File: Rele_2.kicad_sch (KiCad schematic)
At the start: 5 parts

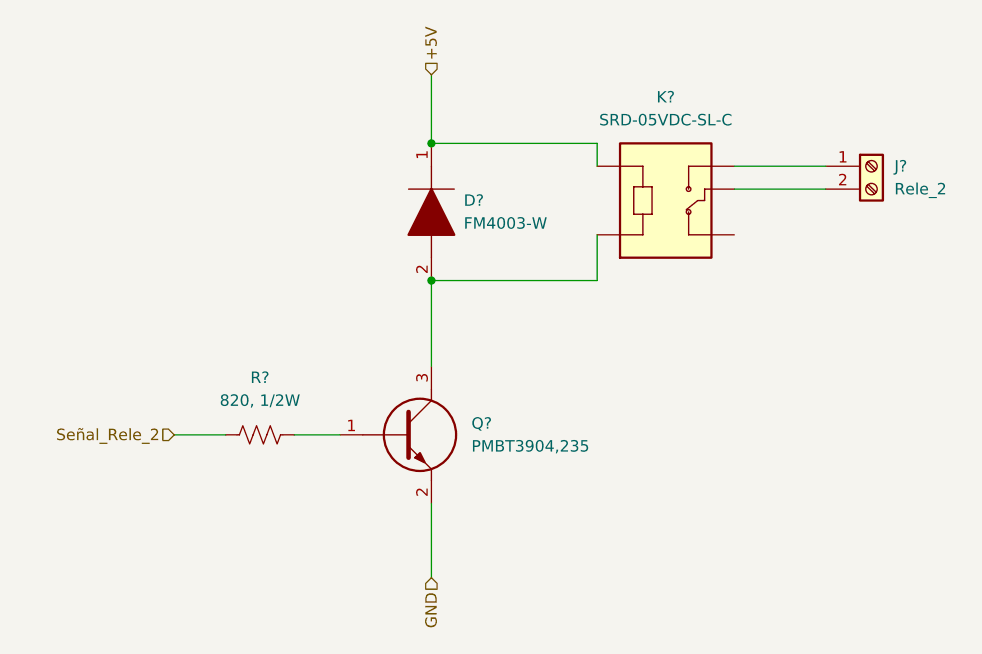
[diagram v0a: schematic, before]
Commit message: Ajuste del esquematico
Se cambio el integrado ESP32 por 2 tiras de pines de 1x15, se quitaron los switches EN y BOOT que ya estan en el NodeMCU, se quito el mutliplexor 74HC y se cablearon las I/O
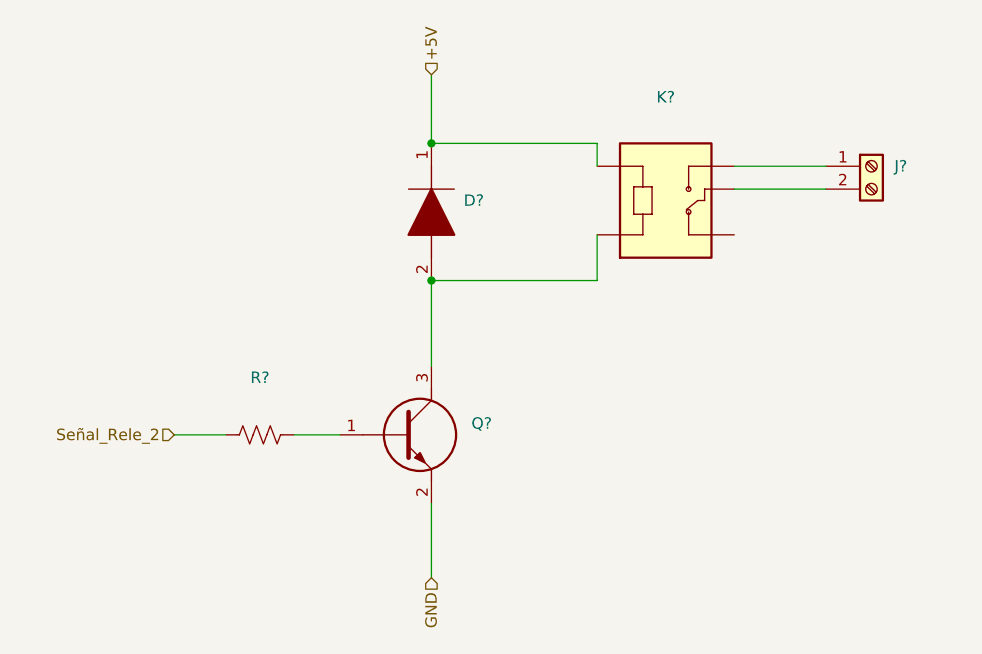
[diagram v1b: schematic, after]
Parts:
- D?: value FM4003-W -> (none); footprint DIOM5025X231N -> (none)
- J?: value Rele_2 -> (none)
- K?: value SRD-05VDC-SL-C -> (none); footprint RELAY_SRD-05VDC-SL-C -> (none)
- Q?: value PMBT3904,235 -> (none); footprint SOT95P230X110-3N -> (none)
- R?: value 820, 1/2W -> (none)
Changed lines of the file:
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@@
       (effects (font (size 1.27 1.27)) (justify left))
     )
-    (property "Value" "FM4003-W" (id 1) (at 142.6464 81.2799 90)
+    (property "Value" "" (id 1) (at 142.6464 81.2799 90)
       (effects (font (size 1.27 1.27)) (justify left))
     )
-    (property "Footprint" "DIOM5025X231N" (id 2) (at 139.065 83.82 0)
+    (property "Footprint" "" (id 2) (at 139.065 83.82 0)
       (effects (font (size 1.27 1.27)) (justify left) hide)
     )
@@
       (effects (font (size 1.27 1.27)) (justify left))
     )
-    (property "Value" "Rele_2" (id 1) (at 190.5 77.4699 0)
+    (property "Value" "" (id 1) (at 190.5 77.4699 0)
       (effects (font (size 1.27 1.27)) (justify left))
     )
@@
     (in_bom yes) (on_board yes) (fields_autoplaced)
     (property "Reference" "K?" (id 0) (at 165.1 67.2592 0))
-    (property "Value" "SRD-05VDC-SL-C" (id 1) (at 165.1 69.7992 0))
-    (property "Footprint" "RELAY_SRD-05VDC-SL-C" (id 2) (at 165.1 77.47 0)
+    (property "Value" "" (id 1) (at 165.1 69.7992 0))
+    (property "Footprint" "" (id 2) (at 165.1 77.47 0)
       (effects (font (size 1.27 1.27)) (justify left bottom) hide)
     )
@@
       (effects (font (size 1.27 1.27)) (justify left))
     )
-    (property "Value" "PMBT3904,235" (id 1) (at 143.51 106.0449 0)
+    (property "Value" "" (id 1) (at 143.51 106.0449 0)
       (effects (font (size 1.27 1.27)) (justify left))
     )
-    (property "Footprint" "SOT95P230X110-3N" (id 2) (at 142.875 108.585 0)
+    (property "Footprint" "" (id 2) (at 142.875 108.585 0)
       (effects (font (size 1.27 1.27)) (justify left) hide)
     )
@@
     (in_bom yes) (on_board yes) (fields_autoplaced)
     (property "Reference" "R?" (id 0) (at 120.015 98.425 90))
-    (property "Value" "820, 1/2W" (id 1) (at 120.015 100.965 90))
+    (property "Value" "" (id 1) (at 120.015 100.965 90))
     (property "Footprint" "" (id 2) (at 120.269 103.759 90)
       (effects (font (size 1.27 1.27)) hide)

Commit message: Modificación de posición de circ. filtrado y circ. de adaptación de tensión
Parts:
- D?, J?, K?, Q?, R?: value (none) -> ~
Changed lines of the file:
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@@
       (effects (font (size 1.27 1.27)) (justify left))
     )
-    (property "Value" "" (id 1) (at 142.6464 81.2799 90)
+    (property "Value" "~" (id 1) (at 142.6464 81.2799 90)
       (effects (font (size 1.27 1.27)) (justify left))
     )
@@
       (effects (font (size 1.27 1.27)) (justify left))
     )
-    (property "Value" "" (id 1) (at 190.5 77.4699 0)
+    (property "Value" "~" (id 1) (at 190.5 77.4699 0)
       (effects (font (size 1.27 1.27)) (justify left))
     )
@@
     (in_bom yes) (on_board yes) (fields_autoplaced)
     (property "Reference" "K?" (id 0) (at 165.1 67.2592 0))
-    (property "Value" "" (id 1) (at 165.1 69.7992 0))
+    (property "Value" "~" (id 1) (at 165.1 69.7992 0))
     (property "Footprint" "" (id 2) (at 165.1 77.47 0)
       (effects (font (size 1.27 1.27)) (justify left bottom) hide)
@@
       (effects (font (size 1.27 1.27)) (justify left))
     )
-    (property "Value" "" (id 1) (at 143.51 106.0449 0)
+    (property "Value" "~" (id 1) (at 143.51 106.0449 0)
       (effects (font (size 1.27 1.27)) (justify left))
     )
@@
     (in_bom yes) (on_board yes) (fields_autoplaced)
     (property "Reference" "R?" (id 0) (at 120.015 98.425 90))
-    (property "Value" "" (id 1) (at 120.015 100.965 90))
+    (property "Value" "~" (id 1) (at 120.015 100.965 90))
     (property "Footprint" "" (id 2) (at 120.269 103.759 90)
       (effects (font (size 1.27 1.27)) hide)

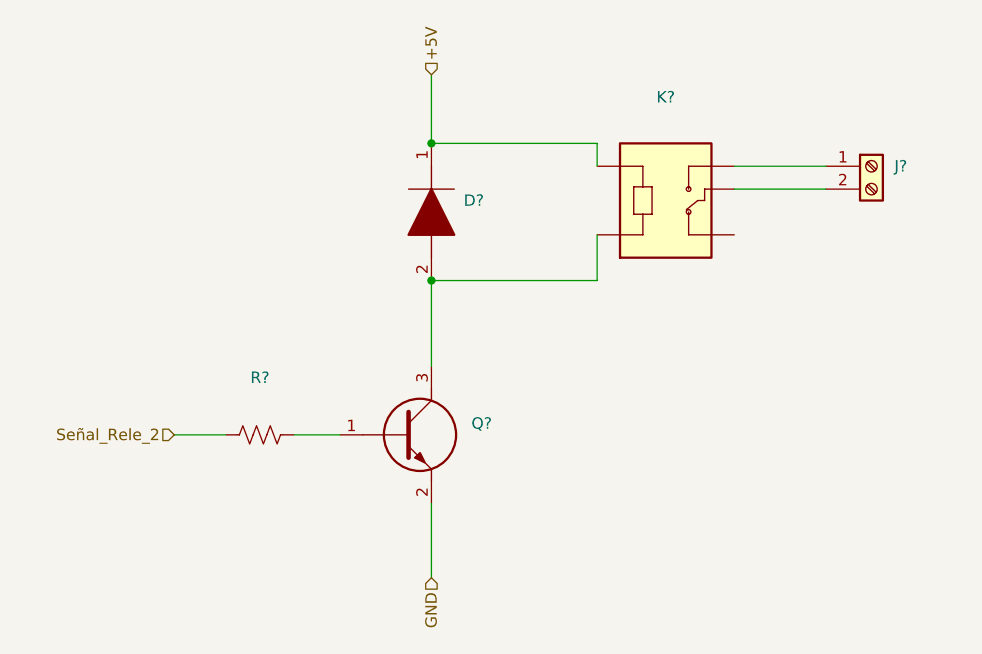
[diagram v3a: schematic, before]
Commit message: Actualización de SCH según placa industrial, y búsqueda de footprints.
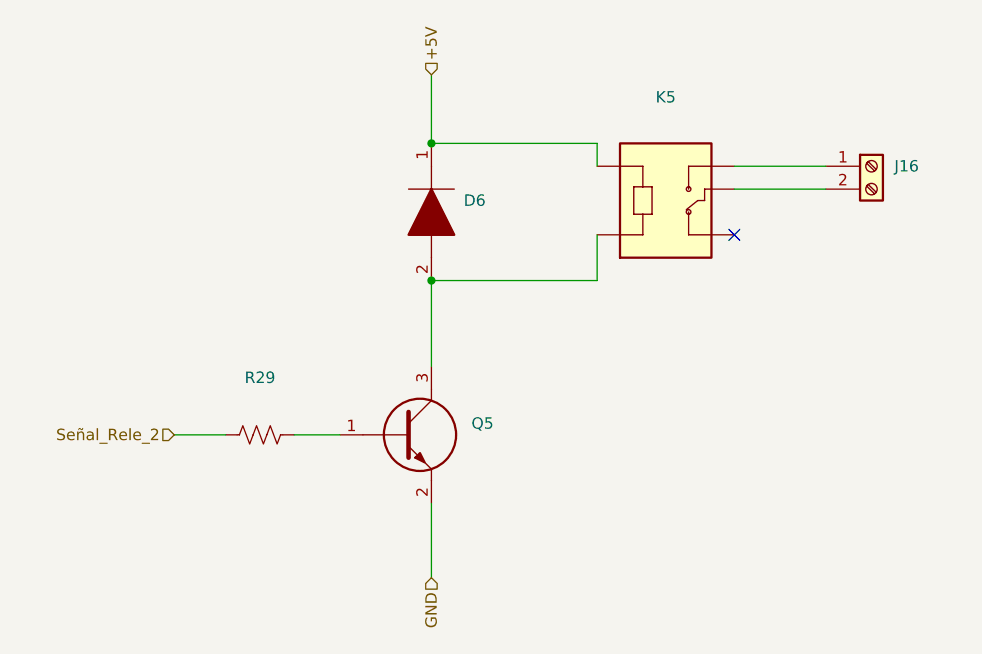
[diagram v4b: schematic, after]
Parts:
- D6: renamed from D?; value ~ -> (none)
- J16: renamed from J?; value ~ -> (none)
- K5: renamed from K?; value ~ -> (none)
- Q5: renamed from Q?; value ~ -> (none)
- R29: renamed from R?; value ~ -> (none)
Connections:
- no-connect marks 0 -> 1
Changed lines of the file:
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@@
   (junction (at 139.065 87.63) (diameter 0) (color 0 0 0 0)
   )
+  (no_connect (at 172.72 82.55))
   (wire (pts (xy 139.065 72.39) (xy 157.48 72.39))
     (stroke (width 0) (type default) (color 0 0 0 0))
@@
   (symbol (lib_id "FM4003-W:FM4003-W") (at 139.065 72.39 270) (unit 1)
     (in_bom yes) (on_board yes) (fields_autoplaced)
-    (property "Reference" "D?" (id 0) (at 142.6464 78.7399 90)
+    (property "Reference" "D6" (id 0) (at 142.6464 78.7399 90)
       (effects (font (size 1.27 1.27)) (justify left))
     )
-    (property "Value" "~" (id 1) (at 142.6464 81.2799 90)
+    (property "Value" "" (id 1) (at 142.6464 81.2799 90)
       (effects (font (size 1.27 1.27)) (justify left))
     )
@@
   (symbol (lib_id "Connector:Screw_Terminal_01x02") (at 187.96 74.93 0) (unit 1)
     (in_bom yes) (on_board yes) (fields_autoplaced)
-    (property "Reference" "J?" (id 0) (at 190.5 74.9299 0)
+    (property "Reference" "J16" (id 0) (at 190.5 74.9299 0)
       (effects (font (size 1.27 1.27)) (justify left))
     )
-    (property "Value" "~" (id 1) (at 190.5 77.4699 0)
+    (property "Value" "" (id 1) (at 190.5 77.4699 0)
       (effects (font (size 1.27 1.27)) (justify left))
     )
@@
   (symbol (lib_id "SRD-05VDC-SL-C:SRD-05VDC-SL-C") (at 165.1 77.47 0) (unit 1)
     (in_bom yes) (on_board yes) (fields_autoplaced)
-    (property "Reference" "K?" (id 0) (at 165.1 67.2592 0))
-    (property "Value" "~" (id 1) (at 165.1 69.7992 0))
+    (property "Reference" "K5" (id 0) (at 165.1 67.2592 0))
+    (property "Value" "" (id 1) (at 165.1 69.7992 0))
     (property "Footprint" "" (id 2) (at 165.1 77.47 0)
       (effects (font (size 1.27 1.27)) (justify left bottom) hide)
@@
   (symbol (lib_id "PMBT3904,235:PMBT3904,235") (at 128.905 104.775 0) (unit 1)
     (in_bom yes) (on_board yes) (fields_autoplaced)
-    (property "Reference" "Q?" (id 0) (at 143.51 103.5049 0)
+    (property "Reference" "Q5" (id 0) (at 143.51 103.5049 0)
       (effects (font (size 1.27 1.27)) (justify left))
     )
-    (property "Value" "~" (id 1) (at 143.51 106.0449 0)
+    (property "Value" "" (id 1) (at 143.51 106.0449 0)
       (effects (font (size 1.27 1.27)) (justify left))
     )
@@
   (symbol (lib_id "Device:R_US") (at 120.015 104.775 90) (unit 1)
     (in_bom yes) (on_board yes) (fields_autoplaced)
-    (property "Reference" "R?" (id 0) (at 120.015 98.425 90))
-    (property "Value" "~" (id 1) (at 120.015 100.965 90))
+    (property "Reference" "R29" (id 0) (at 120.015 98.425 90))
+    (property "Value" "" (id 1) (at 120.015 100.965 90))
     (property "Footprint" "" (id 2) (at 120.269 103.759 90)
       (effects (font (size 1.27 1.27)) hide)

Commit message: Fin de SCH, config de inicio para PCB
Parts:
- D6: value (none) -> FM4003-W; footprint (none) -> FM4003W:DIOM5025X231N
- J16: value (none) -> Rele_2; footprint (none) -> TB002-500-02BE:TB00250002BE
- K5: value (none) -> SRD-05VDC-SL-C; footprint (none) -> SRD-05VDC-SL-C-Version_2:RELAY_SRD-05VDC-SL-C
- Q5: value (none) -> PMBT3904,235; footprint (none) -> PMBT3904,235:SOT95P230X110-3N
- R29: value (none) -> 820, 1/2W; footprint (none) -> Resistor_SMD:R_0805_2012Metric
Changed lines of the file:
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@@
       (effects (font (size 1.27 1.27)) (justify left))
     )
-    (property "Value" "" (id 1) (at 142.6464 81.2799 90)
+    (property "Value" "FM4003-W" (id 1) (at 142.6464 81.2799 90)
       (effects (font (size 1.27 1.27)) (justify left))
     )
-    (property "Footprint" "" (id 2) (at 139.065 83.82 0)
+    (property "Footprint" "FM4003W:DIOM5025X231N" (id 2) (at 139.065 83.82 0)
       (effects (font (size 1.27 1.27)) (justify left) hide)
     )
@@
       (effects (font (size 1.27 1.27)) (justify left))
     )
-    (property "Value" "" (id 1) (at 190.5 77.4699 0)
+    (property "Value" "Rele_2" (id 1) (at 190.5 77.4699 0)
       (effects (font (size 1.27 1.27)) (justify left))
     )
-    (property "Footprint" "" (id 2) (at 187.96 74.93 0)
+    (property "Footprint" "TB002-500-02BE:TB00250002BE" (id 2) (at 187.96 74.93 0)
       (effects (font (size 1.27 1.27)) hide)
     )
@@
     (in_bom yes) (on_board yes) (fields_autoplaced)
     (property "Reference" "K5" (id 0) (at 165.1 67.2592 0))
-    (property "Value" "" (id 1) (at 165.1 69.7992 0))
-    (property "Footprint" "" (id 2) (at 165.1 77.47 0)
+    (property "Value" "SRD-05VDC-SL-C" (id 1) (at 165.1 69.7992 0))
+    (property "Footprint" "SRD-05VDC-SL-C-Version_2:RELAY_SRD-05VDC-SL-C" (id 2) (at 165.1 77.47 0)
       (effects (font (size 1.27 1.27)) (justify left bottom) hide)
     )
@@
       (effects (font (size 1.27 1.27)) (justify left))
     )
-    (property "Value" "" (id 1) (at 143.51 106.0449 0)
+    (property "Value" "PMBT3904,235" (id 1) (at 143.51 106.0449 0)
       (effects (font (size 1.27 1.27)) (justify left))
     )
-    (property "Footprint" "" (id 2) (at 142.875 108.585 0)
+    (property "Footprint" "PMBT3904,235:SOT95P230X110-3N" (id 2) (at 142.875 108.585 0)
       (effects (font (size 1.27 1.27)) (justify left) hide)
     )
@@
     (in_bom yes) (on_board yes) (fields_autoplaced)
     (property "Reference" "R29" (id 0) (at 120.015 98.425 90))
-    (property "Value" "" (id 1) (at 120.015 100.965 90))
-    (property "Footprint" "" (id 2) (at 120.269 103.759 90)
+    (property "Value" "820, 1/2W" (id 1) (at 120.015 100.965 90))
+    (property "Footprint" "Resistor_SMD:R_0805_2012Metric" (id 2) (at 120.269 103.759 90)
       (effects (font (size 1.27 1.27)) hide)
     )

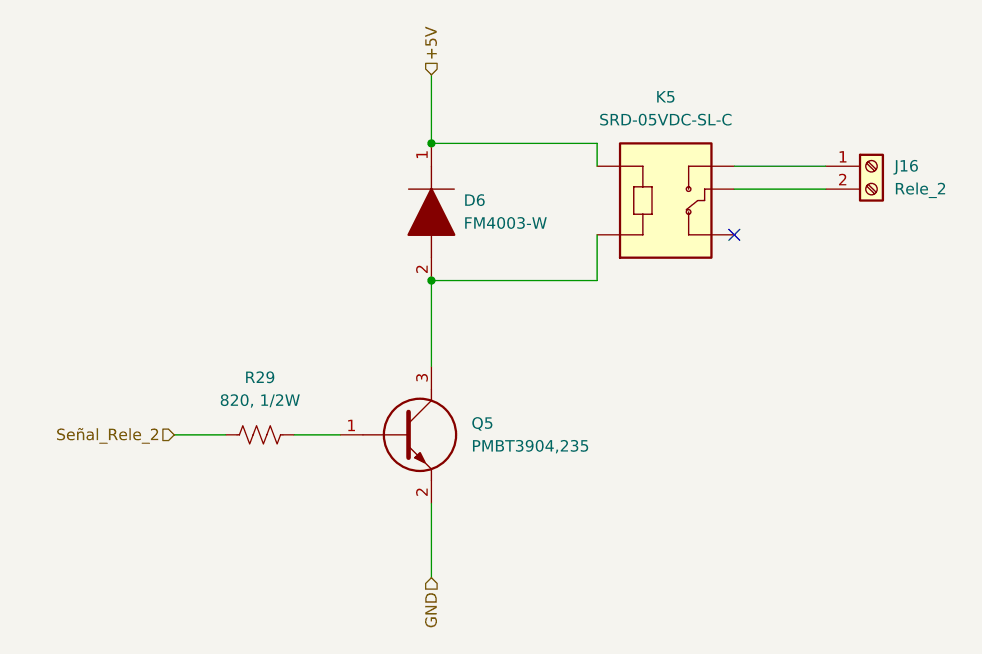
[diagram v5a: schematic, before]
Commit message: Cambios en SCH y PCB.
Se cambio el adaptador de nivel 5-3,3V por un circuito con MOSFET 2N7002, dado que ya no hay stock del NXB. Se modificó el footprint del expansor I/O por uno thorugh-hole.
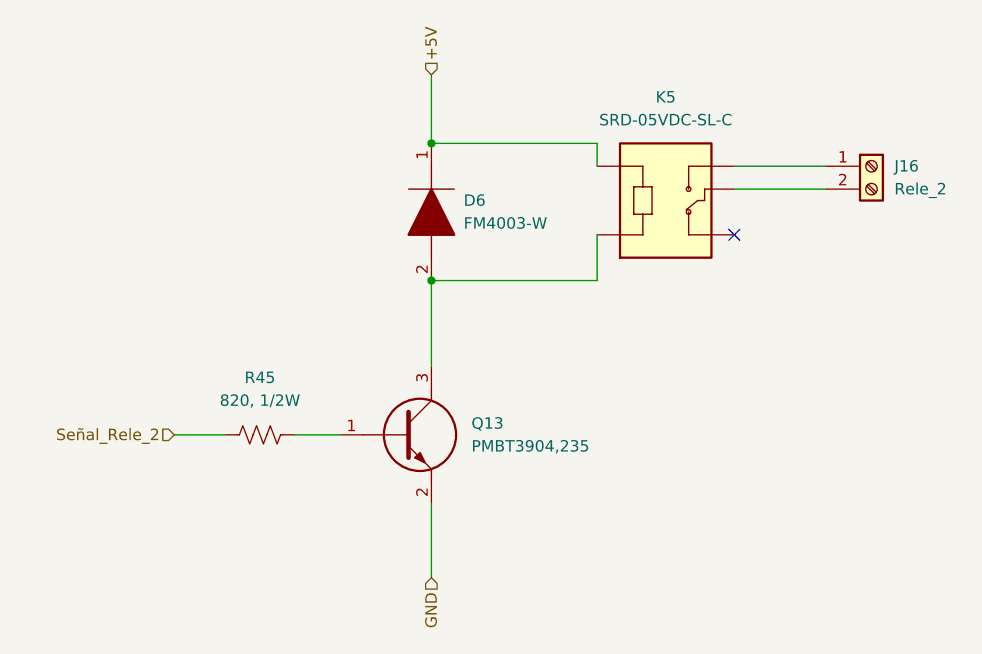
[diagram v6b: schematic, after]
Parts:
- renumbered Q5 to Q13, R29 to R45
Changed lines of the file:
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@@
   (symbol (lib_id "PMBT3904,235:PMBT3904,235") (at 128.905 104.775 0) (unit 1)
     (in_bom yes) (on_board yes) (fields_autoplaced)
-    (property "Reference" "Q5" (id 0) (at 143.51 103.5049 0)
+    (property "Reference" "Q13" (id 0) (at 143.51 103.5049 0)
       (effects (font (size 1.27 1.27)) (justify left))
     )
@@
   (symbol (lib_id "Device:R_US") (at 120.015 104.775 90) (unit 1)
     (in_bom yes) (on_board yes) (fields_autoplaced)
-    (property "Reference" "R29" (id 0) (at 120.015 98.425 90))
+    (property "Reference" "R45" (id 0) (at 120.015 98.425 90))
     (property "Value" "820, 1/2W" (id 1) (at 120.015 100.965 90))
     (property "Footprint" "Resistor_SMD:R_0805_2012Metric" (id 2) (at 120.269 103.759 90)

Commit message: Se finalizó con el PCB del prototipo.
Dado que se buscó a toda costa que el PCB fuera de 1 capa, en varios puntos del circuito se tuvieron que agregar pin headers individuales para conectar a 3V3 y GND, junto con tiras de pin headers. Cada una de estas se conectara luego entre si mediante cables.

Tambien se generaron los archivos Gerber y BOM.
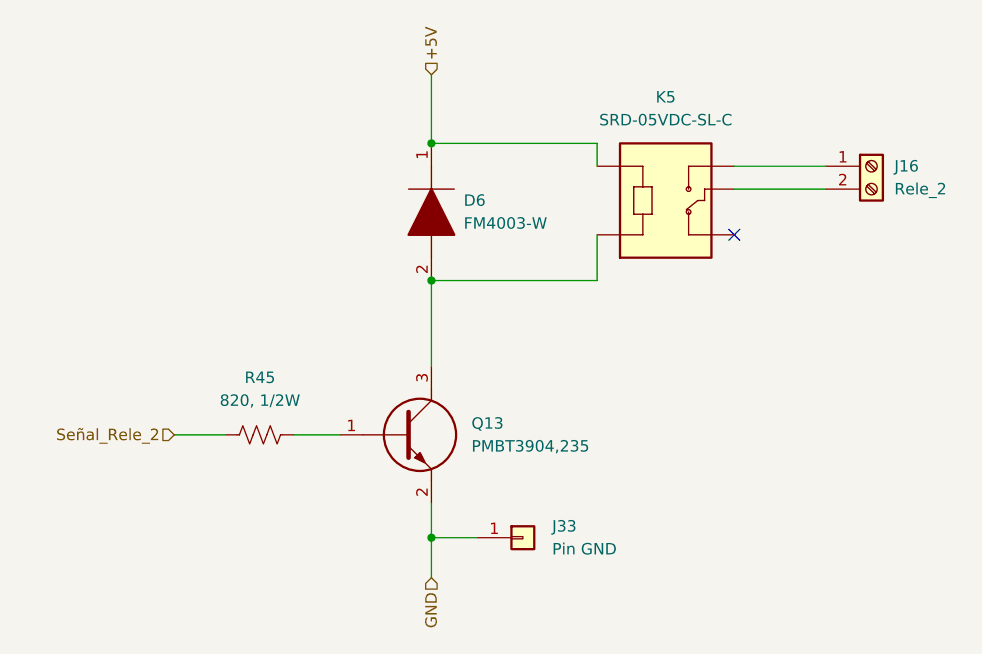
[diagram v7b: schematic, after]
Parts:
- added J33: Pin GND, Connector_PinHeader_2.54mm:PinHeader_1x01_P2.54mm_Vertical, symbol Connector_Generic:Conn_01x01
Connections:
- net GND: now also J33.1 (Pin_1)
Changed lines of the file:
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@@
 (kicad_sch (version 20211123) (generator eeschema)
   (paper "A4")
+  (junction (at 139.065 116.205) (diameter 0) (color 0 0 0 0)
+  )
   (junction (at 139.065 72.39) (diameter 0) (color 0 0 0 0)
   )
@@
     (stroke (width 0) (type default) (color 0 0 0 0))
   )
+  (wire (pts (xy 139.065 116.205) (xy 139.065 120.65))
+    (stroke (width 0) (type default) (color 0 0 0 0))
+  )
   (wire (pts (xy 172.72 77.47) (xy 182.88 77.47))
     (stroke (width 0) (type default) (color 0 0 0 0))
@@
     (stroke (width 0) (type default) (color 0 0 0 0))
   )
-  (wire (pts (xy 139.065 112.395) (xy 139.065 120.65))
+  (wire (pts (xy 139.065 116.205) (xy 144.145 116.205))
+    (stroke (width 0) (type default) (color 0 0 0 0))
+  )
+  (wire (pts (xy 139.065 112.395) (xy 139.065 116.205))
     (stroke (width 0) (type default) (color 0 0 0 0))
   )
@@
     (pin "2")
   )
+  (symbol (lib_id "Connector_Generic:Conn_01x01") (at 149.225 116.205 0) (unit 1)
+    (in_bom yes) (on_board yes) (fields_autoplaced)
+    (property "Reference" "J33" (id 0) (at 152.4762 114.9349 0)
+      (effects (font (size 1.27 1.27)) (justify left))
+    )
+    (property "Value" "Pin GND" (id 1) (at 152.4762 117.4749 0)
+      (effects (font (size 1.27 1.27)) (justify left))
+    )
+    (property "Footprint" "Connector_PinHeader_2.54mm:PinHeader_1x01_P2.54mm_Vertical" (id 2) (at 149.225 116.205 0)
+      (effects (font (size 1.27 1.27)) hide)
+    )
+    (property "Datasheet" "~" (id 3) (at 149.225 116.205 0)
+      (effects (font (size 1.27 1.27)) hide)
+    )
+    (pin "1")
+  )
   (symbol (lib_id "SRD-05VDC-SL-C:SRD-05VDC-SL-C") (at 165.1 77.47 0) (unit 1)
